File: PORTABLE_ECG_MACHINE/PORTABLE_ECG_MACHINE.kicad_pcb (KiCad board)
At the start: 2 copper layers, 57 parts, among them IC1 AD8232ACPZ, J1 USB_B_Micro, J2 Li-Ion 3.7 CONN, J3 UART, Q1 BSS138, Q2 BSS138, SW1 SW_SPDT, U1 CP2102-GM, U3 TC1262-33, U4 SSD1306

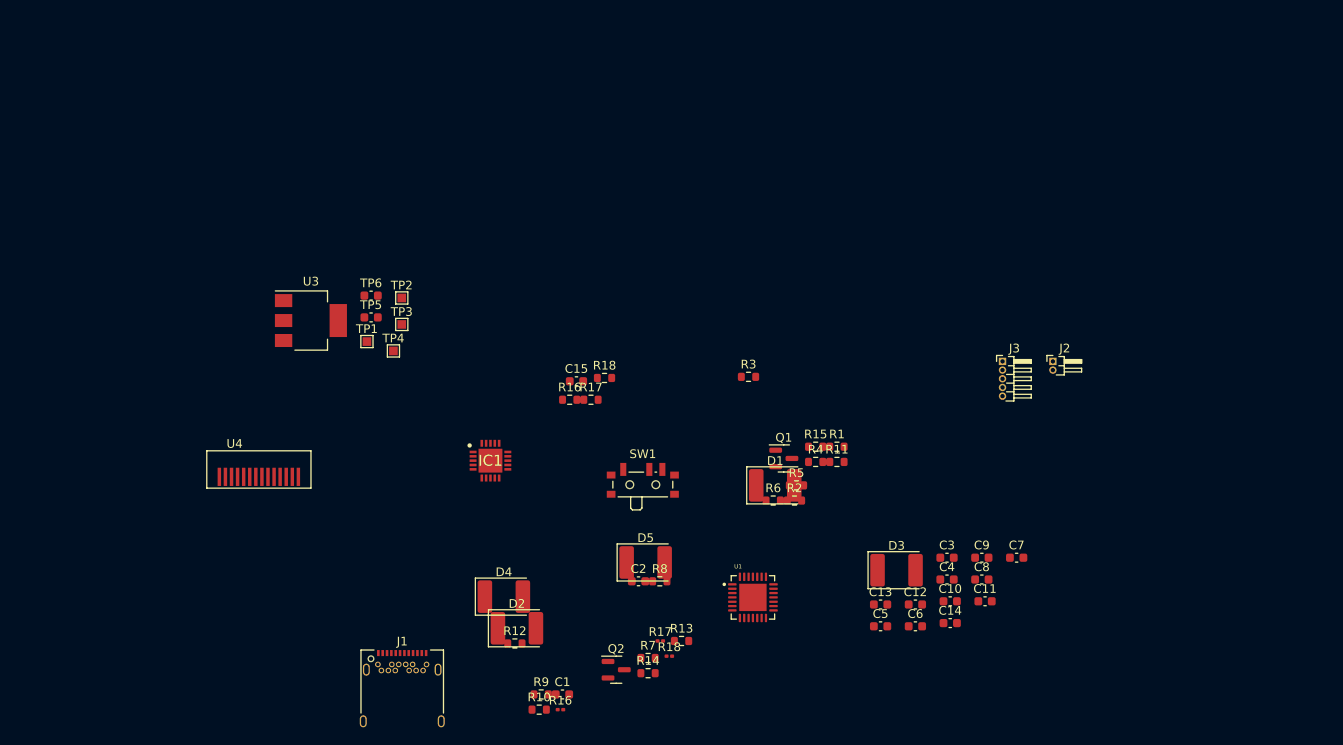
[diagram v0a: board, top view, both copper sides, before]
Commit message: OLED-INSTR_AMP-LION_CHAR-UART EESCHEMA UPDATE | PCBNEW ROUGH ARANGE
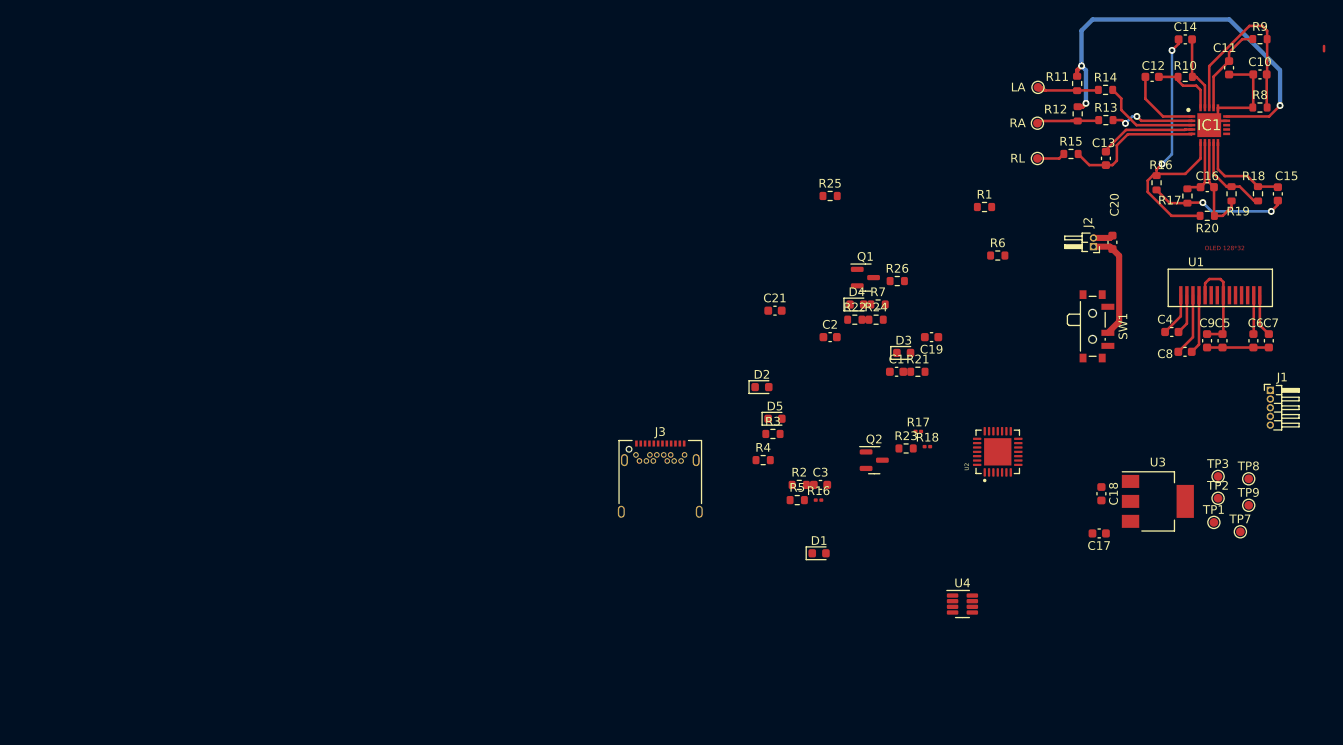
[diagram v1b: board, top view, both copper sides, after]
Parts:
- added C10: .1uf, Capacitor_SMD:C_0603_1608Metric, F.Cu at (216.4, 24.1)
- added C11: .1uf, Capacitor_SMD:C_0603_1608Metric, F.Cu at (212.8, 23.3)
- added C12: 4.7uf, Capacitor_SMD:C_0603_1608Metric, F.Cu at (204.0, 24.4)
- added C14: 4.7uf, Capacitor_SMD:C_0603_1608Metric, F.Cu at (207.8, 20.1)
- added C15: 2.7nf, Capacitor_SMD:C_0603_1608Metric, F.Cu at (218.4, 37.9)
- added C16: 6.8nf, Capacitor_SMD:C_0603_1608Metric, F.Cu at (210.3, 37.1)
- added LA: LA, TestPoint:TestPoint_Pad_D1.0mm, F.Cu at (190.8, 25.6)
- added R10: 10M, Resistor_SMD:R_0603_1608Metric, F.Cu at (207.8, 24.4)
- added R16: 10M, Resistor_SMD:R_0603_1608Metric, F.Cu at (204.5, 36.6)
- added R17: 10M, Resistor_SMD:R_0603_1608Metric, F.Cu at (208.0, 38.1)
- added R18: 1M, Resistor_SMD:R_0603_1608Metric, F.Cu at (216.2, 37.8)
- added R19: 330K, Resistor_SMD:R_0603_1608Metric, F.Cu at (213.1, 37.8)
- added R20: 100K, Resistor_SMD:R_0603_1608Metric, F.Cu at (210.3, 40.4)
- added R8: 10M, Resistor_SMD:R_0603_1608Metric, F.Cu at (216.4, 27.9)
- added R9: 10M, Resistor_SMD:R_0603_1608Metric, F.Cu at (216.4, 20.0)
- added RA: RA, TestPoint:TestPoint_Pad_D1.0mm, F.Cu at (190.8, 29.7)
- added RL: RL, TestPoint:TestPoint_Pad_D1.0mm, F.Cu at (190.8, 33.8)
- added U4: TP4056, Package_TO_SOT_SMD:TSOT-23-8, F.Cu at (182.1, 85.1)
- D1: renamed from D3; footprint Diode_SMD:D_2114_3652Metric -> Diode_SMD:D_0603_1608Metric
- D2: renamed from D4; footprint Diode_SMD:D_2114_3652Metric -> LED_SMD:LED_0603_1608Metric
- D3: renamed from D5; footprint Diode_SMD:D_2114_3652Metric -> LED_SMD:LED_0603_1608Metric
- D4: renamed from D1; footprint Diode_SMD:D_2114_3652Metric -> Diode_SMD:D_0603_1608Metric
- D5: renamed from D2; footprint Diode_SMD:D_2114_3652Metric -> Diode_SMD:D_0603_1608Metric
- TP1: footprint TestPoint:TestPoint_Pad_1.0x1.0mm -> TestPoint:TestPoint_Pad_D1.0mm
- TP2: renamed from TP5; footprint Capacitor_SMD:C_0603_1608Metric -> TestPoint:TestPoint_Pad_D1.0mm
- TP3: renamed from TP6; footprint Capacitor_SMD:C_0603_1608Metric -> TestPoint:TestPoint_Pad_D1.0mm
- TP7: renamed from TP4; footprint TestPoint:TestPoint_Pad_1.0x1.0mm -> TestPoint:TestPoint_Pad_D1.0mm
- TP8: renamed from TP2; footprint TestPoint:TestPoint_Pad_1.0x1.0mm -> TestPoint:TestPoint_Pad_D1.0mm
- TP9: renamed from TP3; footprint TestPoint:TestPoint_Pad_1.0x1.0mm -> TestPoint:TestPoint_Pad_D1.0mm
- moved U1 112.7 mm to (211.8, 49.5)
- moved TP1 99.7 mm to (211.1, 75.7)
- moved TP2 99.7 mm to (211.6, 72.9)
- moved TP3 99.7 mm to (211.6, 70.4)
- moved TP7 99.7 mm to (214.1, 76.8)
- moved TP8 99.7 mm to (215.1, 70.7)
- moved TP9 99.7 mm to (215.1, 73.7)
- moved U3 99.7 mm to (204.6, 73.3)
- moved IC1 91.3 mm to (210.5, 29.9)
- moved R11 84.0 mm to (195.3, 25.1), turned to -90 degrees
- moved R14 69.2 mm to (198.6, 25.9)
- moved C13 66.2 mm to (198.6, 33.8), turned to 90 degrees
- moved R13 64.9 mm to (198.6, 29.4)
- moved R15 64.3 mm to (194.6, 33.3)
- moved SW1 55.1 mm to (197.4, 53.1), turned to -90 degrees
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- renumbered C2 to C1, C15 to C13, C8 to C17, C7 to C18, C6 to C19, C4 to C2, C3 to C20, C5 to C21, C1 to C3, C9 to C4, C12 to C5, C13 to C6, C14 to C7, C10 to C8, C11 to C9, J3 to J1, J1 to J3, R14 to R11, R15 to R12, R18 to R13, R17 to R14, R16 to R15, R9 to R2, R8 to R21, R6 to R22, R7 to R23, R2 to R24, R3 to R25, R4 to R26, R12 to R3, R13 to R4, R10 to R5, R11 to R6, R5 to R7, U4 to U1, U1 to U2
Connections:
- IC1 pad 1: unconnected-(IC1-Pad1) -> Net-(C12-Pad1)
- IC1 pad 10: unconnected-(IC1-Pad10) -> Net-(C15-Pad1)
- IC1 pad 11: unconnected-(IC1-Pad11) -> /LDO-
- IC1 pad 12: unconnected-(IC1-Pad12) -> /LDO+
- IC1 pad 13: unconnected-(IC1-Pad13) -> /SDN#
- IC1 pad 14: unconnected-(IC1-Pad14) -> GND
- IC1 pad 15: unconnected-(IC1-Pad15) -> 3.3V
- IC1 pad 16: unconnected-(IC1-Pad16) -> GND
- IC1 pad 17: unconnected-(IC1-Pad17) -> Net-(C11-Pad2)
- IC1 pad 18: unconnected-(IC1-Pad18) -> Net-(C10-Pad2)
- IC1 pad 19: unconnected-(IC1-Pad19) -> Net-(C14-Pad2)
- IC1 pad 20: unconnected-(IC1-Pad20) -> Net-(C12-Pad2)
- IC1 pad 21: unconnected-(IC1-Pad21) -> GND
- IC1 pad 6: unconnected-(IC1-Pad6) -> Net-(C14-Pad1)
- IC1 pad 7: unconnected-(IC1-Pad7) -> Net-(C16-Pad2)
- IC1 pad 8: unconnected-(IC1-Pad8) -> /REF_OUT
- IC1 pad 9: unconnected-(IC1-Pad9) -> Net-(IC1-Pad9)
- J1 pad 3: TXD -> /TXD
- J1 pad 4: TXD -> /RXD
- R11 pad 2: Net-(R14-Pad2) -> /LA
- R12 pad 2: Net-(R15-Pad2) -> /RA
- R13 pad 1: Net-(R15-Pad2) -> /RA
- R14 pad 1: Net-(R14-Pad2) -> /LA
- R15 pad 1: unconnected-(R16-Pad1) -> /RL
- TP2 pad 1: TXD -> /TXD
- TP3 pad 1: TXD -> /RXD
- U2 pad 25: TXD -> /RXD
- U2 pad 26: TXD -> /TXD
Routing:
- net 3.3V: track 0.00 -> 47.7 mm, vias 0 -> 3
- net Net-(C14-Pad1): track 0.00 -> 34.2 mm, vias 0 -> 2
- net GND: track 0.00 -> 25.3 mm
- net Net-(C10-Pad2): track 0.00 -> 22.5 mm
- net Net-(C13-Pad1): track 0.00 -> 16.2 mm
- net Net-(C15-Pad2): track 0.00 -> 15.8 mm, vias 0 -> 2
- net /BATTERY +VE: track 0.00 -> 12.8 mm
- net /REF_OUT: track 0.00 -> 11.8 mm
- net Net-(C5-Pad2): track 0.00 -> 11.6 mm
- net Net-(IC1-Pad3): track 0.00 -> 11.6 mm
- net Net-(C13-Pad2): track 0.00 -> 11.3 mm
- net Net-(C15-Pad1): track 0.00 -> 10.8 mm
- net Net-(C11-Pad2): track 0.00 -> 10.5 mm
- net Net-(IC1-Pad9): track 0.00 -> 10.00 mm
- net Net-(IC1-Pad2): track 0.00 -> 9.78 mm, vias 0 -> 2
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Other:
- board text added: "OLED 128*32"

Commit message: PCBNEW ROUGH STRUCTURE | EDGECUT PR
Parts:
- removed the R16 at (165.5, 73.1)
- removed the R17 at (177.0, 65.2)
- removed the R18 at (178.1, 67.0)
- removed TP7: B-TEMP, TestPoint:TestPoint_Pad_D1.0mm
- moved TP9 126.5 mm to (88.6, 78.3)
- moved TP8 124.6 mm to (90.7, 78.3)
- moved TP2 123.3 mm to (88.3, 74.7), turned to -90 degrees
- moved TP3 123.2 mm to (88.4, 72.0)
- moved C11 113.6 mm to (99.3, 26.6)
- moved C16 113.6 mm to (96.8, 40.3)
- moved IC1 113.6 mm to (97.0, 33.2)
- moved R12 113.6 mm to (81.9, 31.9)
- moved R17 113.6 mm to (94.5, 41.4)
- moved R20 113.6 mm to (96.8, 43.6)
- moved TP4 113.6 mm to (77.3, 28.8)
- moved C10 113.6 mm to (102.8, 27.4)
- moved C13 113.6 mm to (85.1, 37.0)
- moved C14 113.6 mm to (94.2, 23.3)
- moved C15 113.6 mm to (104.9, 41.1)
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- renumbered LA to TP4, RA to TP5, RL to TP6
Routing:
- net 3.3V: track 47.7 -> 90.6 mm, vias 3 -> 4
- net GND: track 25.3 -> 61.1 mm, vias 0 -> 2
- net Net-(D3-Pad2): track 0.00 -> 19.9 mm, vias 0 -> 2
- net Net-(R24-Pad2): track 0.00 -> 19.6 mm
- net SCL_3.3: track 0.00 -> 15.7 mm, vias 0 -> 2
- net Net-(D3-Pad1): track 0.00 -> 12.2 mm, vias 0 -> 2
- net SDA_3.3: track 0.00 -> 10.3 mm, vias 0 -> 2
- net Net-(C21-Pad1): track 0.00 -> 10.0 mm
- net USB_D-: track 0.00 -> 9.49 mm
- net VIN: track 0.00 -> 8.95 mm
- net USB_D+: track 0.00 -> 8.16 mm
- net Net-(R1-Pad2): track 0.00 -> 7.74 mm
- net Net-(C1-Pad1): track 0.00 -> 7.42 mm
- net Net-(R26-Pad2): track 0.00 -> 7.21 mm
- net Net-(D2-Pad1): track 0.00 -> 6.74 mm
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
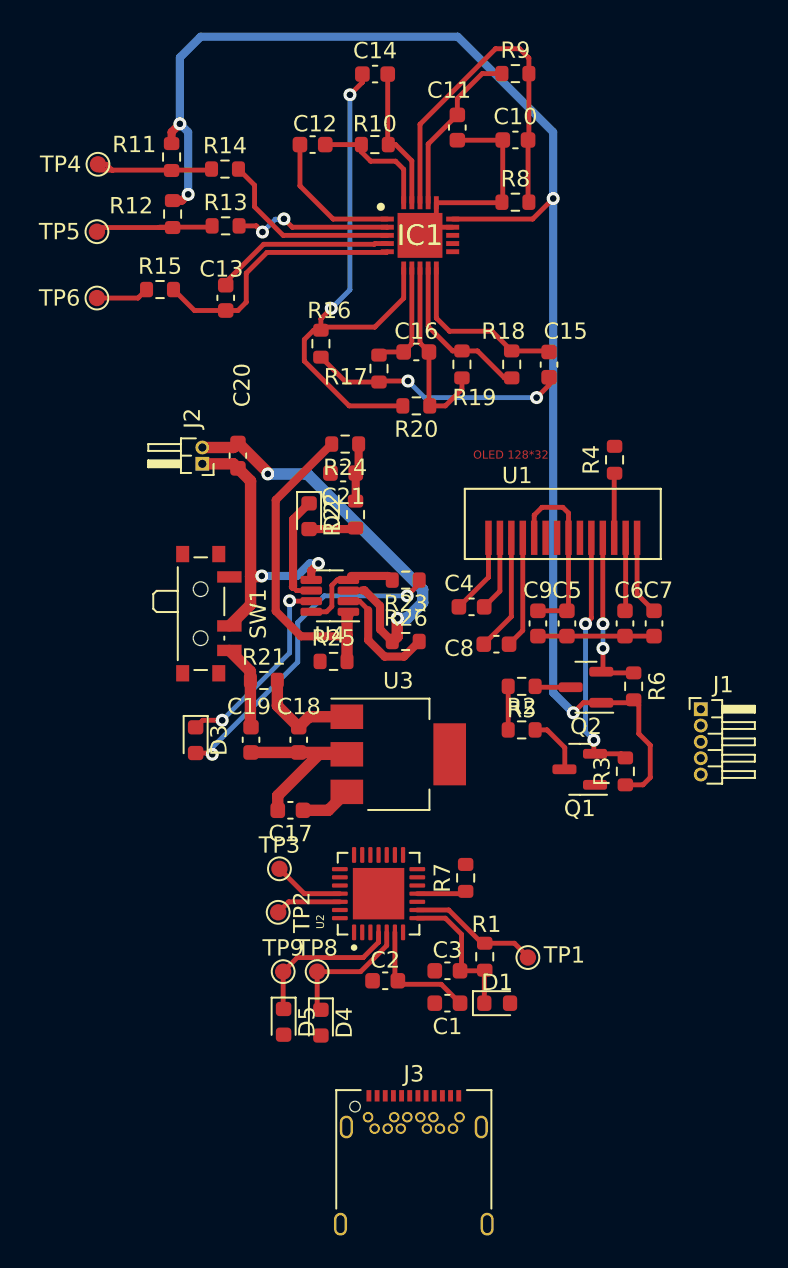
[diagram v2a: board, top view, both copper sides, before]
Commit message: PCBNEW edgecut update| compact rough design
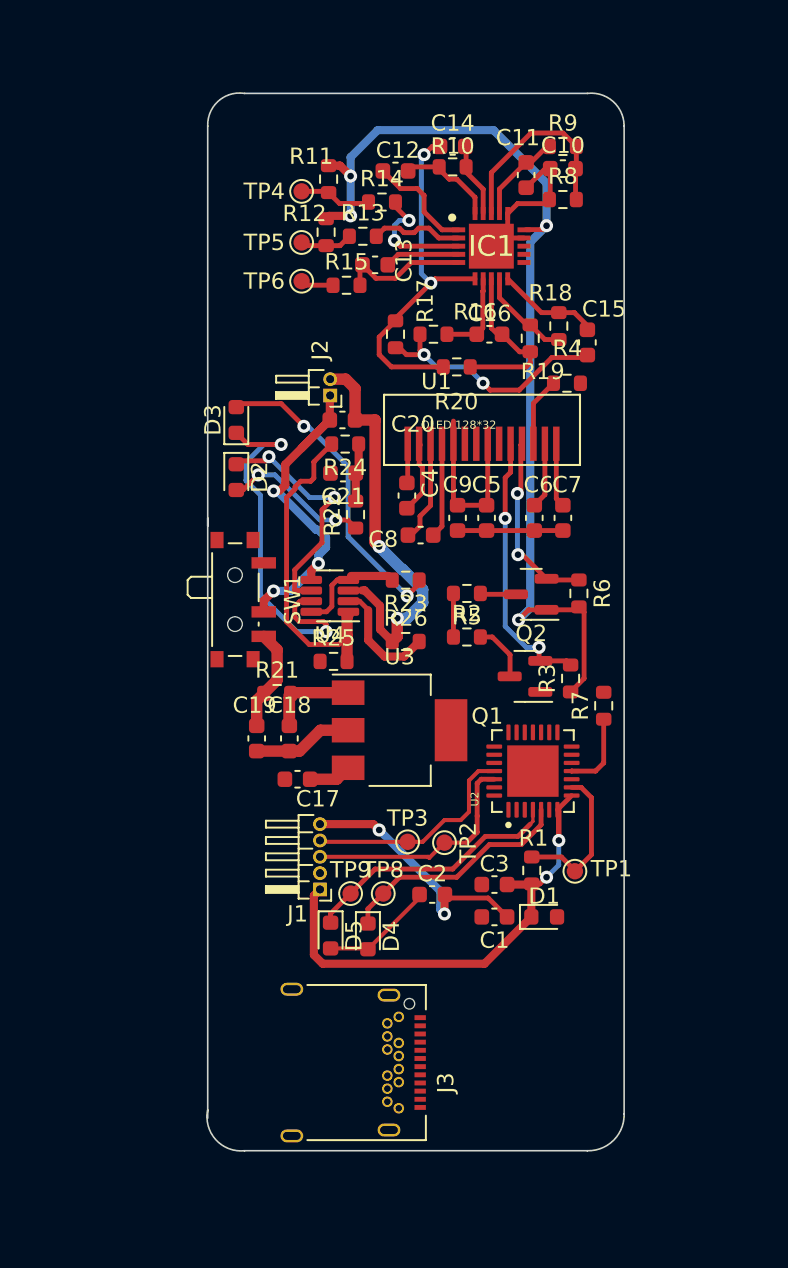
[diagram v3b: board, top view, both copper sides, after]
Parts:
- moved J1 25.8 mm to (90.9, 73.2), turned to 180 degrees
- moved D3 19.8 mm to (85.8, 44.5), turned to 90 degrees
- moved R7 13.5 mm to (108.2, 62.0)
- moved TP4 12.6 mm to (89.8, 30.5)
- moved TP6 12.6 mm to (89.8, 36.0)
- moved TP5 12.6 mm to (89.8, 33.6)
- moved U2 12.1 mm to (103.9, 66.0)
- moved R15 11.4 mm to (92.5, 36.2)
- moved TP2 11.0 mm to (98.5, 70.4)
- moved R14 9.82 mm to (94.7, 31.2)
- moved R11 9.71 mm to (91.4, 29.8)
- moved R12 9.46 mm to (91.2, 33.0)
- moved C13 9.37 mm to (94.2, 35.0), turned to 0 degrees
- moved J2 8.88 mm to (91.5, 43.0)
- moved C7 8.54 mm to (105.8, 50.5)
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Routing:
- net 3.3V: track 90.6 -> 59.6 mm
- net VIN: track 8.95 -> 31.2 mm, vias 0 -> 2
- net Net-(C14-Pad1): track 34.2 -> 22.1 mm
- net Net-(D3-Pad1): track 12.2 -> 23.4 mm
- net /TXD: track 4.04 -> 14.5 mm
- net Net-(C10-Pad2): track 22.5 -> 12.3 mm
- net /RXD: track 4.33 -> 13.6 mm
- net Net-(C1-Pad1): track 7.42 -> 16.4 mm, vias 0 -> 2
- net Net-(C13-Pad1): track 16.2 -> 7.95 mm
- net Net-(D2-Pad1): track 6.74 -> 14.9 mm, vias 0 -> 2
- net Net-(C13-Pad2): track 11.3 -> 4.61 mm
- net USB_D-: track 9.49 -> 16.0 mm
- net USB_D+: track 8.16 -> 14.6 mm
- net Net-(D2-Pad2): track 2.87 -> 9.12 mm, vias 0 -> 2
- net Net-(C11-Pad2): track 10.5 -> 5.64 mm
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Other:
- board outline added: 25.5 x 64.8 mm
